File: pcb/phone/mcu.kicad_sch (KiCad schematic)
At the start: 25 parts, among them J1 Conn_01x04, U1 STM32H743ZIT6, Y1 ECS-80-12-33Q-GN-TR

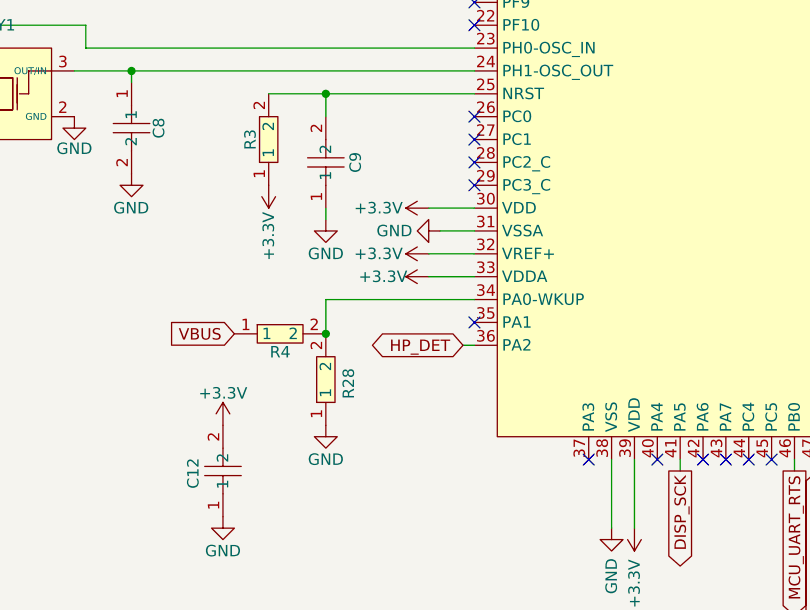
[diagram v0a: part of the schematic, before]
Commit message: Sync docs to schematic refdes + add VDDA ferrite, C20 footprint, completion plan
- Sync 11 doc files to schematic-canonical reference designators (U3->U5 codec,
  U4->U8 buck-boost, U5->U9 LDO, U6->U11 charger, U7->U10 fuel gauge, U8->U3
  TXB0108, U9->U12 SN74AXC4T774, U10->D1 USBLC6-2, U11->U6/U7 ESDA6V1,
  J1->USBC1, J_BATT->CN1, SW1->SW21). Schematic refdes are canonical.
- MCU sheet: add VDDA ferrite bead (L1 BLM18KG601SN1D) + 1uF (C18) + 10nF (C19)
  decoupling per datasheet. Add PWR_FLAG on VDDA for ERC.
- Modem sheet: assign C20 (470uF tantalum) footprint temp_470uf:CAP-SMD_L7.3-W4.3
- Libraries: add new symbols to easyeda2kicad.kicad_sym + passives.kicad_sym
- Add .devin/rules/kicad-mcp-first.md (MCP-first inspection rule)
- Add docs/schematic-completion-plan.md (per-sheet review tracker, 2026-07-28)
- Add pcb/phone/scripts/add_headphone_jack.py (flagged for cleanup in plan §D)

Generated with [Devin](https://devin.ai)

Co-Authored-By: Devin <158243242+devin-ai-integration[bot]@users.noreply.github.com>
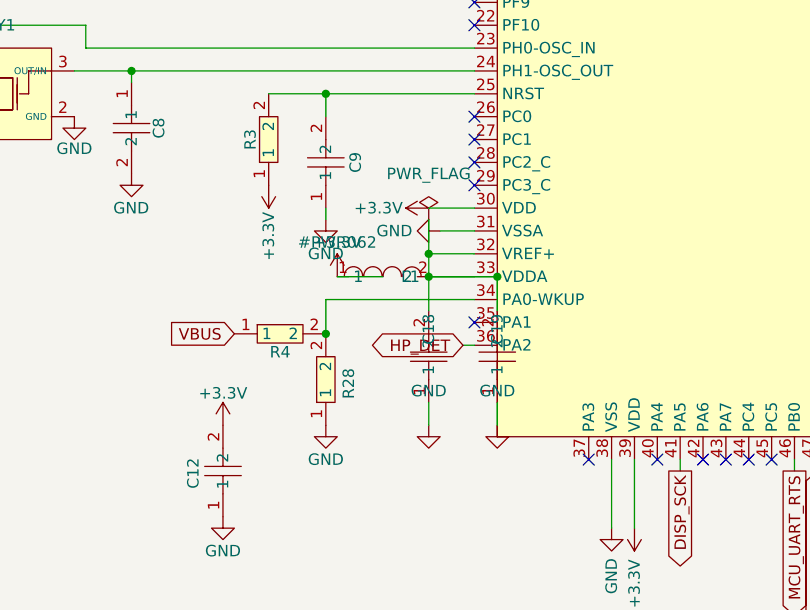
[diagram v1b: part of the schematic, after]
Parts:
- added C18: 1uF, easyeda2kicad:C0603, symbol passives:GRM188R61C105KA93D
- added C19: 10nF, easyeda2kicad:C0603, symbol passives:CC0603KRX7R9BB103
- added L1: BLM18KG601SN1D, easyeda2kicad:L0603, symbol passives:BLM18KG601SN1D
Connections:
- net +3.3V: now also L1.1; no longer U1.32 (VREF+), U1.33 (VDDA)
- net GND: now also C18.1, C19.1
- new net: C18.2, C19.2, L1.2, U1.32 (VREF+), U1.33 (VDDA)

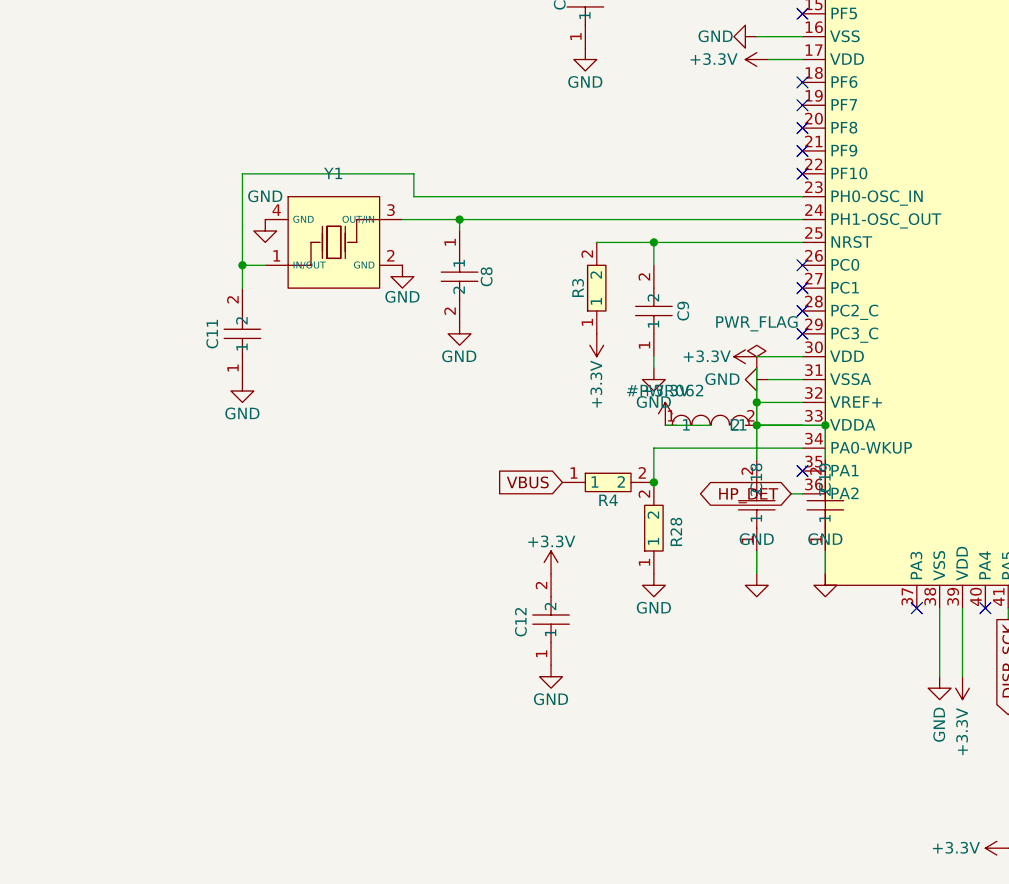
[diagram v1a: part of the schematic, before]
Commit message: Assign footprints to 29 components missing footprint properties
All 28 custom-library components (passives, connectors, ICs) get footprints
from their symbol library defaults. J1 (SWD debug header) gets a standard
KiCad 2.54mm through-hole pin header footprint per user selection.

Footprints assigned:
- C18-C23: easyeda2kicad:C0805 (10uF 0805 caps)
- C24-C26: easyeda2kicad:C0603 (100nF 0603 caps)
- R6-R18: easyeda2kicad:R0603 (0603 resistors)
- J_HINGE2: easyeda2kicad:FPC-SMD_14P-P0.50_HDGC_0.5K-HX-14PWB
- J_MIC1, J_SPK1: easyeda2kicad:CONN-SMD_P2.00_S2B-PH-SM4-TB-LF-SN
- U2: easyeda2kicad:PCIE-SMD_PCIE-52P40H-1 (mini-PCIe)
- U3: easyeda2kicad:TSSOP-20_L6.5-W4.4-P0.65-LS6.4-BL (TXB0108)
- U5: easyeda2kicad:QFN-40_L5.0-W5.0-P0.40-BL-EP3.7 (ALC5651)
- J1: Connector_PinHeader_2.54mm:PinHeader_1x04_P2.54mm_Vertical (SWD)

Also includes KiCad's own metadata updates (title block, sheet ordering,
designator list normalization).

Generated with [Devin](https://devin.ai)

Co-Authored-By: Devin <158243242+devin-ai-integration[bot]@users.noreply.github.com>
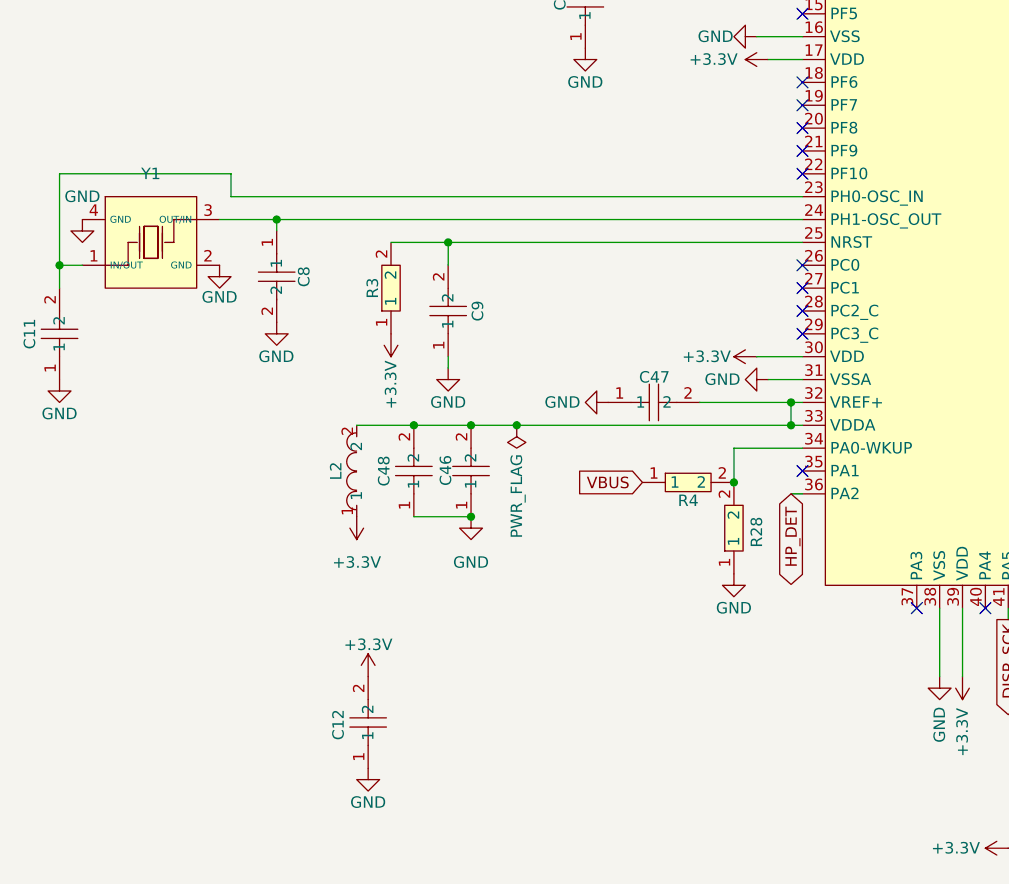
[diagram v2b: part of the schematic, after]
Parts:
- removed C18: 1uF, easyeda2kicad:C0603, symbol passives:GRM188R61C105KA93D
- removed C19: 10nF, easyeda2kicad:C0603, symbol passives:CC0603KRX7R9BB103
- removed L1: BLM18KG601SN1D, easyeda2kicad:L0603, symbol passives:BLM18KG601SN1D
- added C46, C47: CC0603KRX7R9BB104, easyeda2kicad:C0603, symbol passives:CC0603KRX7R9BB104
- added C48: 1uF, easyeda2kicad:C0603, symbol passives:GRM188R61C105KA93D
- added L2: BLM18KG601SN1D, easyeda2kicad:L0603, symbol passives:BLM18KG601SN1D
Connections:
- net +3.3V: now also L2.1
- net GND: now also C46.1, C47.1, C48.1
- net at U1.32 (VREF+), U1.33 (VDDA): now also C46.2, C47.2, C48.2, L2.2
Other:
- moved on the sheet: C11, C12, C8, C9, R28, R3, R4, Y1

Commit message: Re-assign J1 footprint (KiCad overwrote previous edit)
J1 (SWD debug header) footprint was overwritten by KiCad's auto-save.
Re-applied: Connector_PinHeader_2.54mm:PinHeader_1x04_P2.54mm_Vertical

Generated with [Devin](https://devin.ai)

Co-Authored-By: Devin <158243242+devin-ai-integration[bot]@users.noreply.github.com>
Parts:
- J1: footprint (none) -> Connector_PinHeader_2.54mm:PinHeader_1x04_P2.54mm_Vertical
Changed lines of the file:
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@@
 			)
 		)
-		(property "Footprint" ""
+		(property "Footprint" "Connector_PinHeader_2.54mm:PinHeader_1x04_P2.54mm_Vertical"
 			(at 320.04 82.55 0)
 			(hide yes)

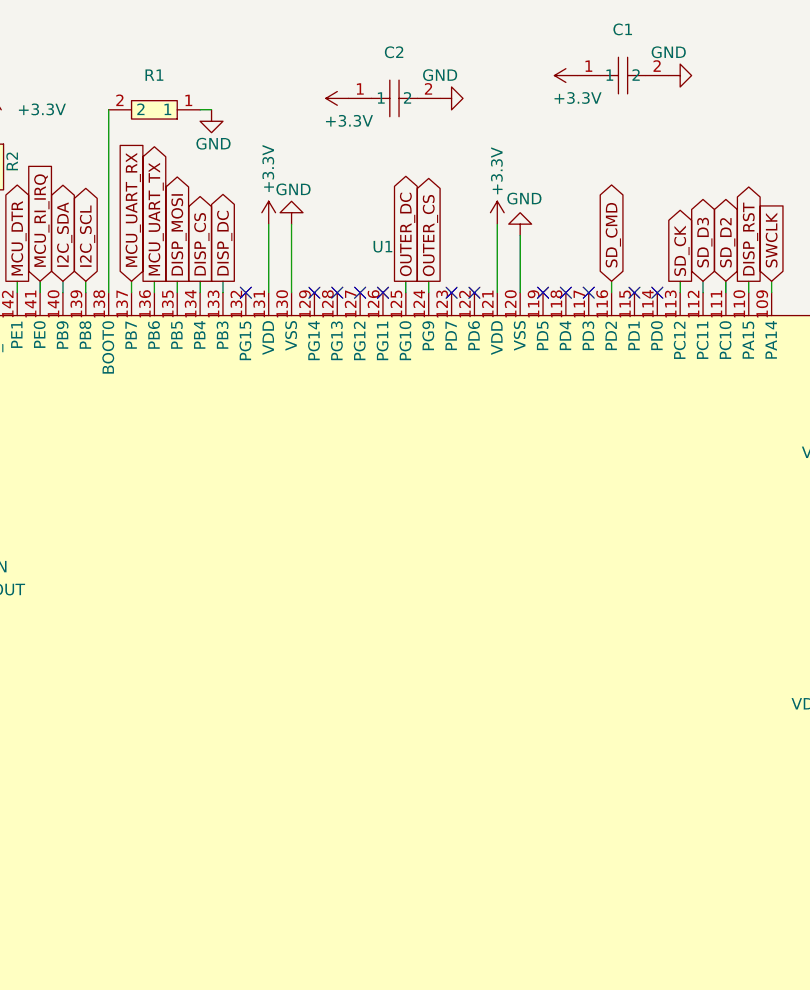
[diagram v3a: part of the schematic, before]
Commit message: Restructure display sheet for candybar + fix pinout + add backlight FET + power switch reversal
Display sheet (LOCKED):
- Fix J_DISP1 pinout to match HS20HS072RX datasheet (was 1/12 correct, now all 14 pins match)
- Add backlight FET circuit: Q1 (AO3400A), R20 (100ohm gate), R5 (10k pulldown), R19 moved to pin 10
- Fix R19 MPN: was 470ohm part with 4.7ohm value, swapped to RC0603JR-074R7L (correct 4.7ohm)
- Move display power from +1V8 to +3.3V (1.8V below VCC min 2.4V)
- Remove display_daughter sheet entry, J_HINGE1, J_HINGE2, OUTER_CS/OUTER_DC
- Add no-connect flags on MCU PG9/PG10 (freed from outer display)
- FPC connector orientation review flagged for PCB layout phase

Power switch (reversed 2026-08-27):
- Move SW21 from battery path back to TPS63021 EN pin (signal-level)
- Select C&K OS102011MA1QN1 (100mA SPDT, LCSC C226259), 8.4mm actuator, usable as finger toggle
- Battery always connected, charging while off restored
- Supersedes 2026-08-17 battery-path architecture

New library parts:
- ics:AO3400A (N-ch MOSFET, SOT-23, LCSC C20917)
- passives:0603WAF1000T5E (100ohm 0603, LCSC C22775)
- passives:RC0603JR-074R7L (4.7ohm 0603, LCSC C137621)
- electromech:OS102011MA1QN1 (SPDT slide switch, LCSC C226259)

Docs updated:
- project-log: 3 new entries (display review, power switch reversal, USB hub)
- bom.md: item 25b switch selected, display backlight parts
- block-diagram.md: +BATT net (no switch), U8 EN pin (switched by SW21)
- schematic-completion-plan.md: display sheet LOCKED, section F complete
- task-tracker.md: O2 updated with 2026-08-27 architecture
- ic-by-ic-review.md: Q3 superseded again, DEF-001 updated
- datasheets/README.md: HS20HS072RX pinout verified, SPI confirmed

Generated with [Devin](https://devin.ai)

Co-Authored-By: Devin <158243242+devin-ai-integration[bot]@users.noreply.github.com>
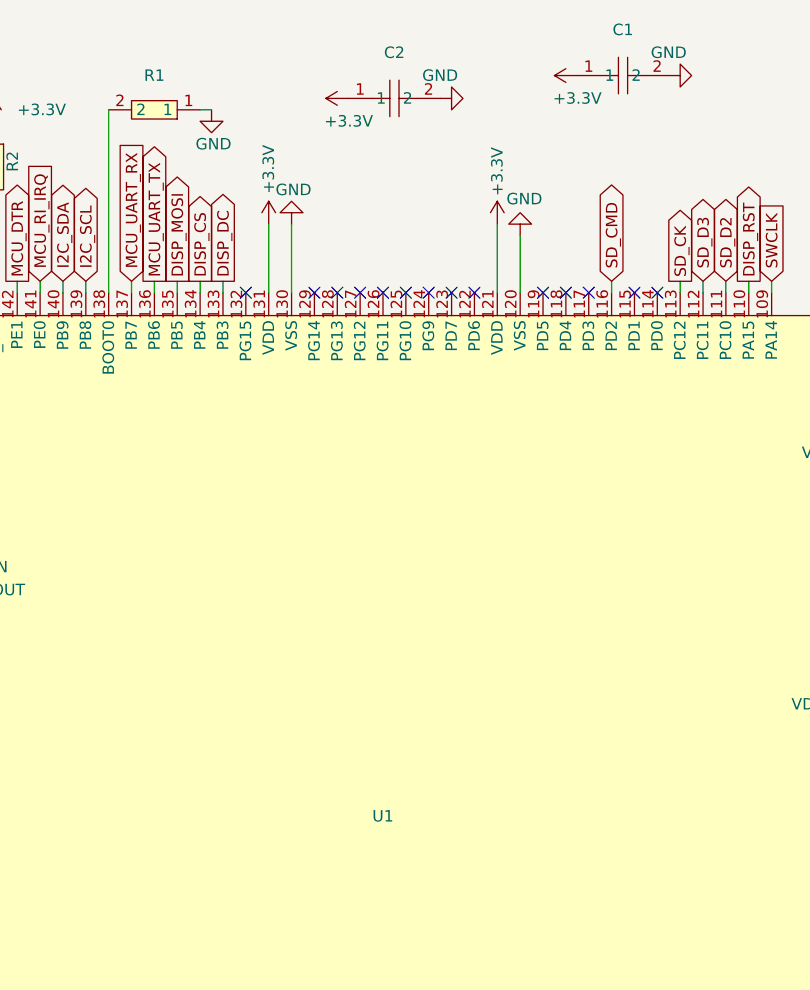
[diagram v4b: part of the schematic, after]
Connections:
- net OUTER_CS: no longer names the net of U1.124 (PG9)
- net OUTER_DC: no longer names the net of U1.125 (PG10)
- no-connect marks 67 -> 69
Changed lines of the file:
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@@
 	)
 	(no_connect
+		(at 228.6 82.55)
+	)
+	(no_connect
 		(at 165.1 110.49)
 	)
@@
 	)
 	(no_connect
+		(at 226.06 82.55)
+	)
+	(no_connect
 		(at 165.1 146.05)
 	)
@@
 	(wire
 		(pts
-			(xy 226.06 81.28) (xy 226.06 82.55)
-		)
-		(stroke
-			(width 0)
-			(type default)
-		)
-	)
-	(wire
-		(pts
 			(xy 195.58 81.28) (xy 195.58 82.55)
 		)
@@
 	(wire
 		(pts
-			(xy 228.6 81.28) (xy 228.6 82.55)
-		)
-		(stroke
-			(width 0)
-			(type default)
-		)
-	)
-	(wire
-		(pts
 			(xy 163.83 95.25) (xy 165.1 95.25)
 		)
@@
 		)
 	)
-	(global_label "OUTER_DC"
-		(shape output)
-		(at 226.06 81.28 90)
-		(fields_autoplaced yes)
-		(effects
-			(font
-				(size 1.27 1.27)
-			)
-			(justify left)
-		)
-		(property "Intersheetrefs" "${INTERSHEET_REFS}"
-			(at 226.06 68.7396 90)
-			(hide yes)
-			(show_name no)
-			(do_not_autoplace no)
-			(effects
-				(font
-					(size 1.27 1.27)
-				)
-				(justify left)
-			)
-		)
-	)
 	(global_label "MCU_UART_CTS"
 		(shape input)
@@
 		)
 	)
-	(global_label "OUTER_CS"
-		(shape output)
-		(at 228.6 81.28 90)
-		(fields_autoplaced yes)
-		(effects
-			(font
-				(size 1.27 1.27)
-			)
-			(justify left)
-		)
-		(property "Intersheetrefs" "${INTERSHEET_REFS}"
-			(at 228.6 68.8001 90)
-			(hide yes)
-			(show_name no)
-			(do_not_autoplace no)
-			(effects
-				(font
-					(size 1.27 1.27)
-				)
-				(justify left)
-			)
-		)
-	)
 	(global_label "MCU_MODEM_RST"
 		(shape output)
@@
 		(in_pos_files yes)
 		(dnp no)
-		(fields_autoplaced yes)
 		(property "Reference" "U1"
-			(at 223.52 77.47 0)
+			(at 223.52 140.716 0)
 			(show_name no)
 			(do_not_autoplace no)
